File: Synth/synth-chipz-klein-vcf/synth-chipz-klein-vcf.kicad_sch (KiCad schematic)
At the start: 57 parts, among them U1 TL074, U2 TL074

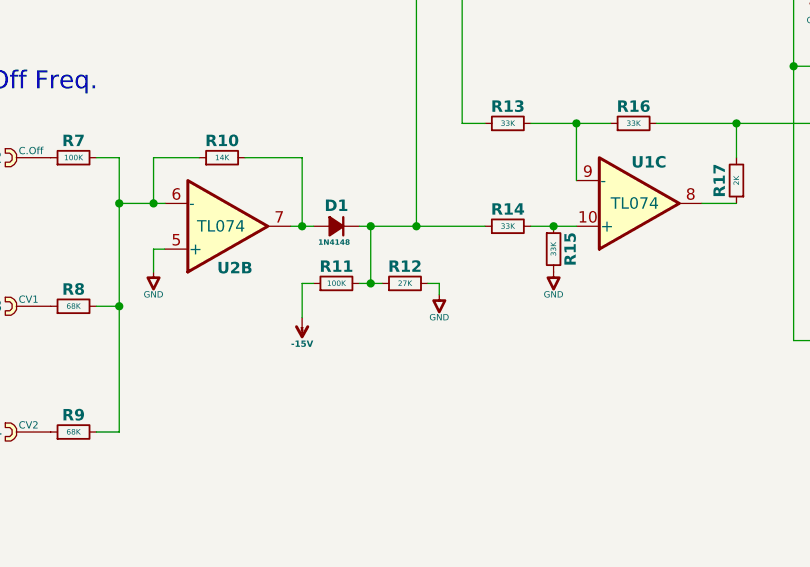
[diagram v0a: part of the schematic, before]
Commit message: Adjust resistor value.
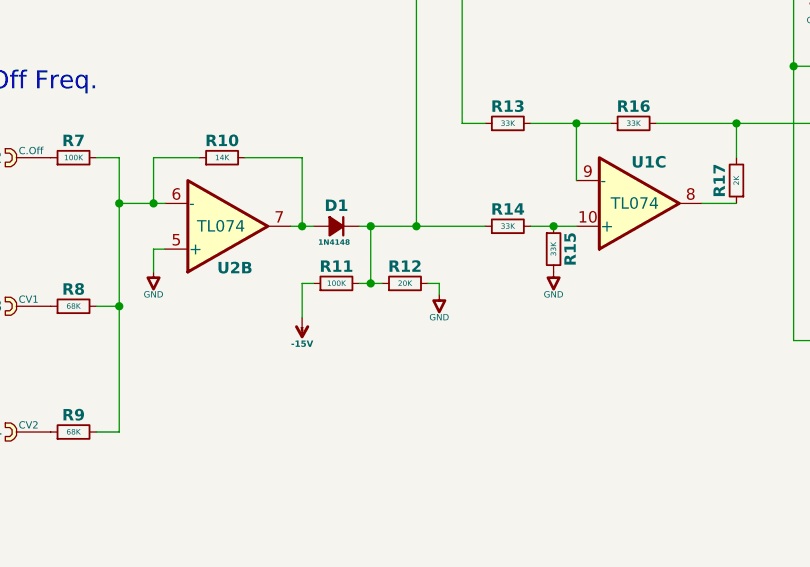
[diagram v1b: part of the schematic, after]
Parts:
- R12: value 27K -> 20K
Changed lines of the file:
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@@
 			)
 		)
-		(property "Value" "27K"
+		(property "Value" "20K"
 			(at 93.98 101.6 90)
 			(do_not_autoplace yes)
